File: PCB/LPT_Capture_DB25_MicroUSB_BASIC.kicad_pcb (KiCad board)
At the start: 2 copper layers, 36 x 20.8 mm, 16 parts, among them J1 USB3155-30-A, J2 DB25P064TXLF, U1 FT245RL

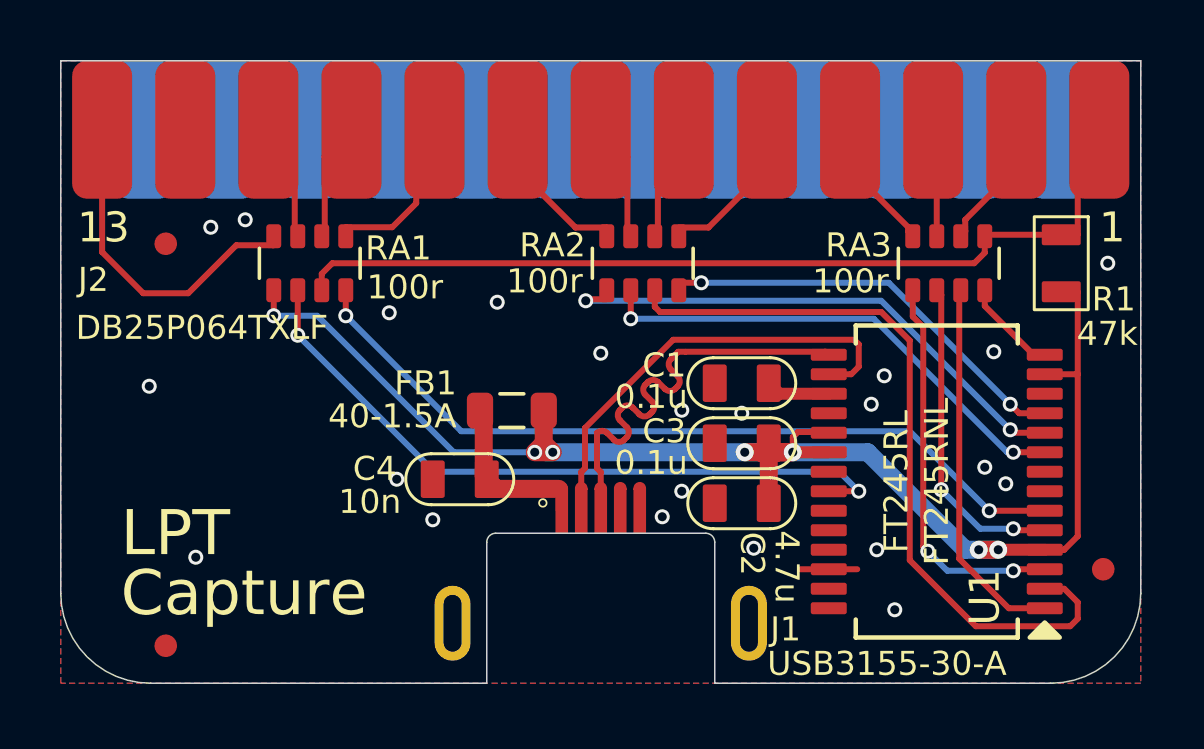
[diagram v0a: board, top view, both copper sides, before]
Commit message: pull db25_microusb_fancy into main
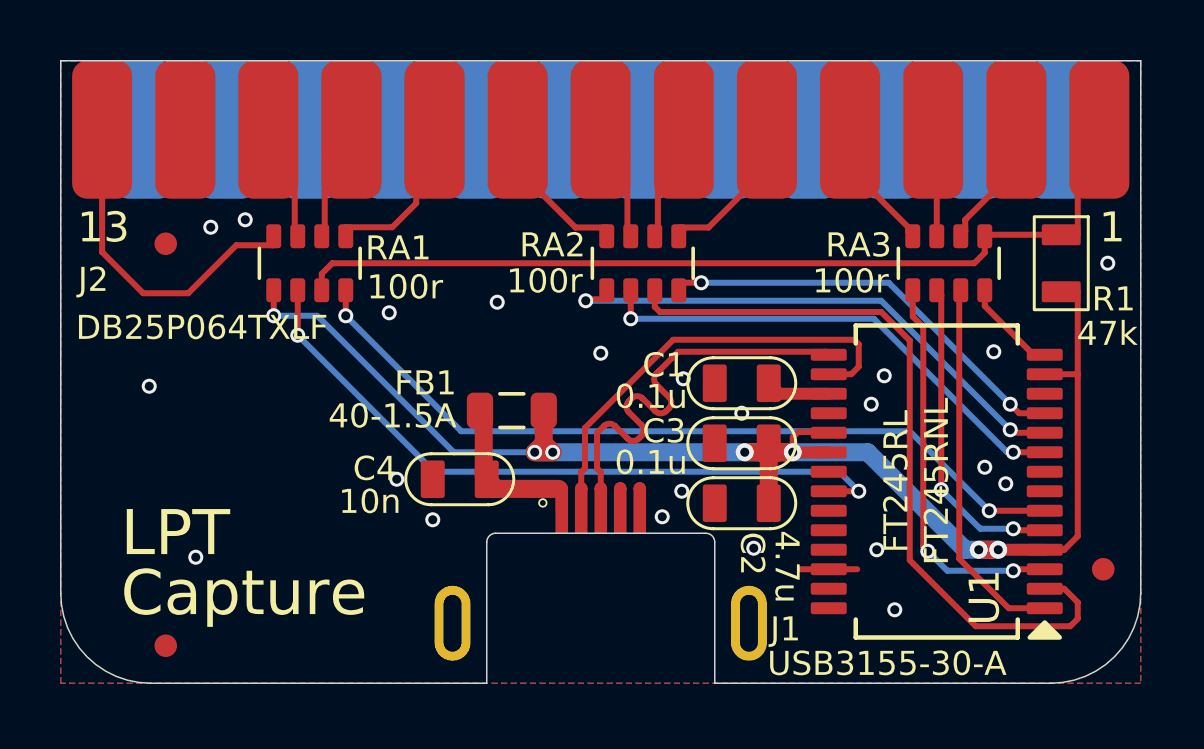
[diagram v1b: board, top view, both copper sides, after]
